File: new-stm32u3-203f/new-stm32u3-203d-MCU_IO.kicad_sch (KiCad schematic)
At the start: 8 parts, among them J7 RESET, SW1 SW_SPDT, U1 STM32U385RGT6Q, X1 32.768kHz

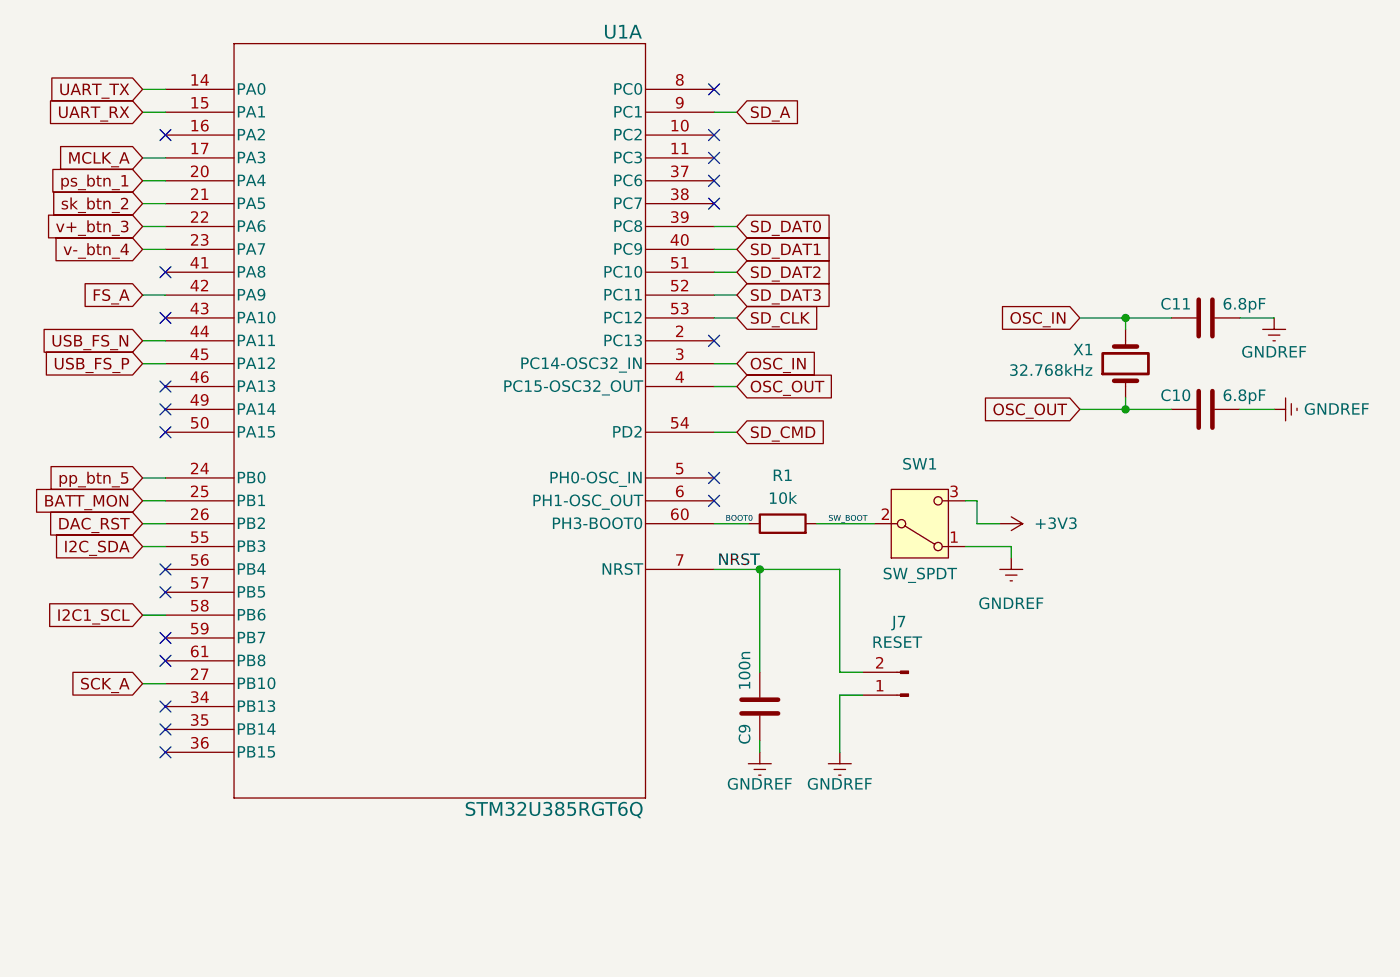
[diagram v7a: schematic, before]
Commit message: restarted routing and started using 6 layers and power planes.
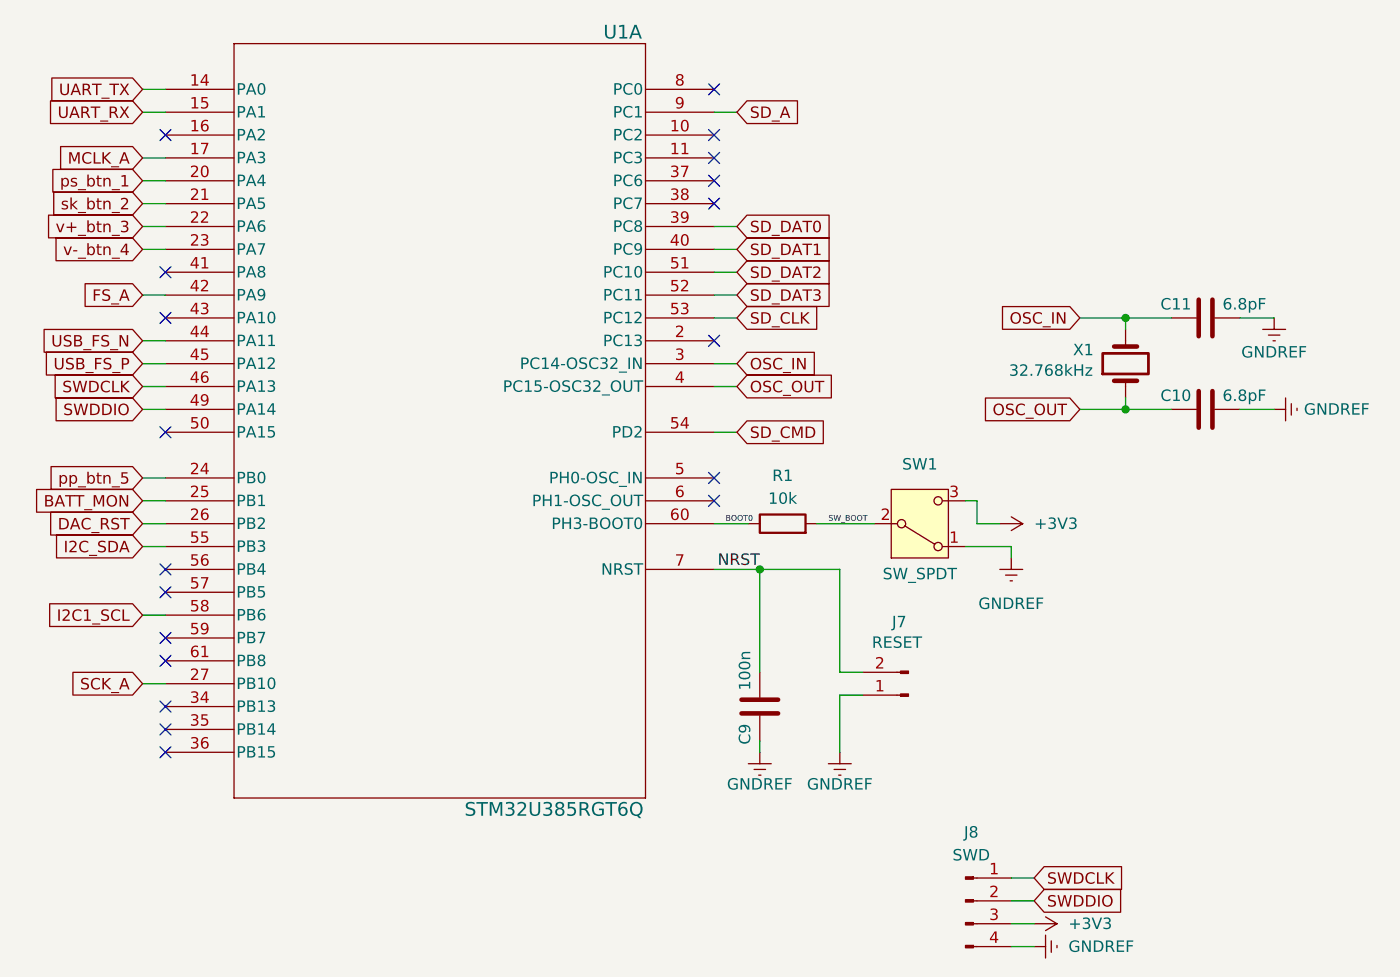
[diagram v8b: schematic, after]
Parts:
- added J8: SWD, Connector_PinHeader_2.54mm:PinHeader_1x04_P2.54mm_Vertical, symbol Connector:Conn_01x04_Pin
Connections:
- net +3V3: now also J8.3 (Pin_3)
- net GNDREF: now also J8.4 (Pin_4)
- net SWDCLK: now reaches U1.46 (PA13)
- net SWDCLK: now also J8.1 (Pin_1)
- net SWDDIO: now reaches U1.49 (PA14)
- net SWDDIO: now also J8.2 (Pin_2)
- no-connect marks 21 -> 19
